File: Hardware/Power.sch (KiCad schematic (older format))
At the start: 38 parts, among them U3 LM2596S-12, U4 LM2596S-5, U5 LM1117-3.3, U6 LM1117-3.3

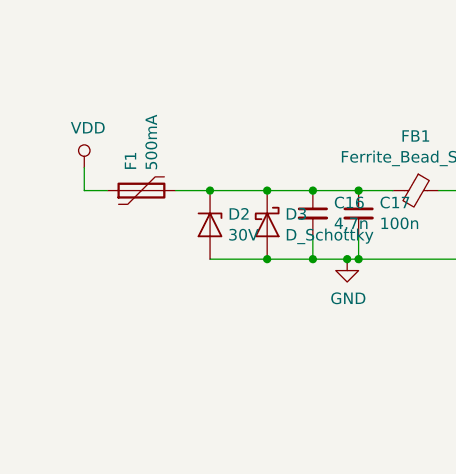
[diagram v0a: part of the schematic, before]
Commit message: passive components changed to 0603 and Main connector configuration set
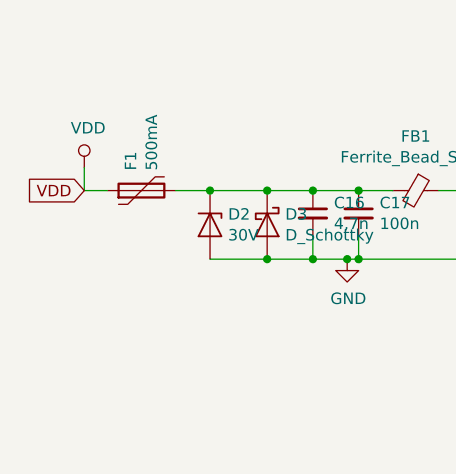
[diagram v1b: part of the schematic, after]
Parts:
- C16, C17, C18, C19, C21, C22, C25, C27, C28, C29, C30: footprint Capacitor_SMD:C_0805_2012Metric -> Capacitor_SMD:C_0603_1608Metric
- C23: footprint Capacitor_SMD:CP_Elec_6.3x5.8 -> Capacitor_SMD:C_0603_1608Metric
- R13, R14, R15, R16, R17, R18: footprint Resistor_SMD:R_0805_2012Metric -> Resistor_SMD:R_0603_1608Metric
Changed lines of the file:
@@
 F 0 "R13" H 3859 1946 50  0000 L CNN
 F 1 "R_Small" H 3859 1855 50  0000 L CNN
-F 2 "Resistor_SMD:R_0805_2012Metric" H 3800 1900 50  0001 C CNN
+F 2 "Resistor_SMD:R_0603_1608Metric" H 3800 1900 50  0001 C CNN
 F 3 "~" H 3800 1900 50  0001 C CNN
 	1    3800 1900
@@
 F 0 "C21" H 4492 2146 50  0000 L CNN
 F 1 "100n" H 4492 2055 50  0000 L CNN
-F 2 "Capacitor_SMD:C_0805_2012Metric" H 4400 2100 50  0001 C CNN
+F 2 "Capacitor_SMD:C_0603_1608Metric" H 4400 2100 50  0001 C CNN
 F 3 "~" H 4400 2100 50  0001 C CNN
 	1    4400 2100
@@
 F 0 "C23" H 6588 2296 50  0000 L CNN
 F 1 "220n" H 6588 2205 50  0000 L CNN
-F 2 "Capacitor_SMD:CP_Elec_6.3x5.8" H 6500 2250 50  0001 C CNN
+F 2 "Capacitor_SMD:C_0603_1608Metric" H 6500 2250 50  0001 C CNN
 F 3 "~" H 6500 2250 50  0001 C CNN
 	1    6500 2250
@@
 F 0 "R16" H 6909 2096 50  0000 L CNN
 F 1 "1k" H 6909 2005 50  0000 L CNN
-F 2 "Resistor_SMD:R_0805_2012Metric" H 6850 2050 50  0001 C CNN
+F 2 "Resistor_SMD:R_0603_1608Metric" H 6850 2050 50  0001 C CNN
 F 3 "~" H 6850 2050 50  0001 C CNN
 	1    6850 2050
@@
 F 0 "C25" H 4492 3346 50  0000 L CNN
 F 1 "100nF" H 4492 3255 50  0000 L CNN
-F 2 "Capacitor_SMD:C_0805_2012Metric" H 4400 3300 50  0001 C CNN
+F 2 "Capacitor_SMD:C_0603_1608Metric" H 4400 3300 50  0001 C CNN
 F 3 "~" H 4400 3300 50  0001 C CNN
 	1    4400 3300
@@
 F 0 "R17" H 6909 3296 50  0000 L CNN
 F 1 "220R" H 6909 3205 50  0000 L CNN
-F 2 "Resistor_SMD:R_0805_2012Metric" H 6850 3250 50  0001 C CNN
+F 2 "Resistor_SMD:R_0603_1608Metric" H 6850 3250 50  0001 C CNN
 F 3 "~" H 6850 3250 50  0001 C CNN
 	1    6850 3250
@@
 F 0 "C27" H 4692 4396 50  0000 L CNN
 F 1 "100n" H 4692 4305 50  0000 L CNN
-F 2 "Capacitor_SMD:C_0805_2012Metric" H 4600 4350 50  0001 C CNN
+F 2 "Capacitor_SMD:C_0603_1608Metric" H 4600 4350 50  0001 C CNN
 F 3 "~" H 4600 4350 50  0001 C CNN
 	1    4600 4350
@@
 F 0 "R18" H 5809 5296 50  0000 L CNN
 F 1 "100k" H 5809 5205 50  0000 L CNN
-F 2 "Resistor_SMD:R_0805_2012Metric" H 5750 5250 50  0001 C CNN
+F 2 "Resistor_SMD:R_0603_1608Metric" H 5750 5250 50  0001 C CNN
 F 3 "~" H 5750 5250 50  0001 C CNN
 	1    5750 5250
@@
 F 0 "R14" V 8096 1950 50  0000 C CNN
 F 1 "900K" V 8005 1950 50  0000 C CNN
-F 2 "Resistor_SMD:R_0805_2012Metric" H 7900 1950 50  0001 C CNN
+F 2 "Resistor_SMD:R_0603_1608Metric" H 7900 1950 50  0001 C CNN
 F 3 "~" H 7900 1950 50  0001 C CNN
 	1    7900 1950
@@
 F 0 "R15" V 8496 1950 50  0000 C CNN
 F 1 "100k" V 8405 1950 50  0000 C CNN
-F 2 "Resistor_SMD:R_0805_2012Metric" H 8300 1950 50  0001 C CNN
+F 2 "Resistor_SMD:R_0603_1608Metric" H 8300 1950 50  0001 C CNN
 F 3 "~" H 8300 1950 50  0001 C CNN
 	1    8300 1950
@@
 F 0 "C22" H 8192 2196 50  0000 L CNN
 F 1 "10n" H 8192 2105 50  0000 L CNN
-F 2 "Capacitor_SMD:C_0805_2012Metric" H 8100 2150 50  0001 C CNN
+F 2 "Capacitor_SMD:C_0603_1608Metric" H 8100 2150 50  0001 C CNN
 F 3 "~" H 8100 2150 50  0001 C CNN
 	1    8100 2150
@@
 F 0 "C16" H 2142 2096 50  0000 L CNN
 F 1 "4,7n" H 2142 2005 50  0000 L CNN
-F 2 "Capacitor_SMD:C_0805_2012Metric" H 2050 2050 50  0001 C CNN
+F 2 "Capacitor_SMD:C_0603_1608Metric" H 2050 2050 50  0001 C CNN
 F 3 "~" H 2050 2050 50  0001 C CNN
 	1    2050 2050
@@
 F 0 "C17" H 2342 2096 50  0000 L CNN
 F 1 "100n" H 2342 2005 50  0000 L CNN
-F 2 "Capacitor_SMD:C_0805_2012Metric" H 2250 2050 50  0001 C CNN
+F 2 "Capacitor_SMD:C_0603_1608Metric" H 2250 2050 50  0001 C CNN
 F 3 "~" H 2250 2050 50  0001 C CNN
 	1    2250 2050
@@
 F 0 "C18" H 2842 2096 50  0000 L CNN
 F 1 "4,7n" H 2842 2005 50  0000 L CNN
-F 2 "Capacitor_SMD:C_0805_2012Metric" H 2750 2050 50  0001 C CNN
+F 2 "Capacitor_SMD:C_0603_1608Metric" H 2750 2050 50  0001 C CNN
 F 3 "~" H 2750 2050 50  0001 C CNN
 	1    2750 2050
@@
 F 0 "C19" H 3042 2096 50  0000 L CNN
 F 1 "100n" H 3042 2005 50  0000 L CNN
-F 2 "Capacitor_SMD:C_0805_2012Metric" H 2950 2050 50  0001 C CNN
+F 2 "Capacitor_SMD:C_0603_1608Metric" H 2950 2050 50  0001 C CNN
 F 3 "~" H 2950 2050 50  0001 C CNN
 	1    2950 2050
@@
 F 0 "C28" H 5592 4396 50  0000 L CNN
 F 1 "100n" H 5592 4305 50  0000 L CNN
-F 2 "Capacitor_SMD:C_0805_2012Metric" H 5500 4350 50  0001 C CNN
+F 2 "Capacitor_SMD:C_0603_1608Metric" H 5500 4350 50  0001 C CNN
 F 3 "~" H 5500 4350 50  0001 C CNN
 	1    5500 4350
@@
 F 0 "C29" H 4692 5246 50  0000 L CNN
 F 1 "100n" H 4692 5155 50  0000 L CNN
-F 2 "Capacitor_SMD:C_0805_2012Metric" H 4600 5200 50  0001 C CNN
+F 2 "Capacitor_SMD:C_0603_1608Metric" H 4600 5200 50  0001 C CNN
 F 3 "~" H 4600 5200 50  0001 C CNN
 	1    4600 5200
@@
 F 0 "C30" H 5592 5246 50  0000 L CNN
 F 1 "100n" H 5592 5155 50  0000 L CNN
-F 2 "Capacitor_SMD:C_0805_2012Metric" H 5500 5200 50  0001 C CNN
+F 2 "Capacitor_SMD:C_0603_1608Metric" H 5500 5200 50  0001 C CNN
 F 3 "~" H 5500 5200 50  0001 C CNN
 	1    5500 5200
@@
 Wire Wire Line
 	4600 5100 4750 5100
+Text GLabel 1050 1950 0    50   Input ~ 0
+VDD
 $EndSCHEMATC
